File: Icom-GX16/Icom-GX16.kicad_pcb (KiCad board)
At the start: 2 copper layers, 27.3 x 30.5 mm, 6 parts, among them J1 Mic Input, J2 Base Board, J3 Headphone/Speaker Input

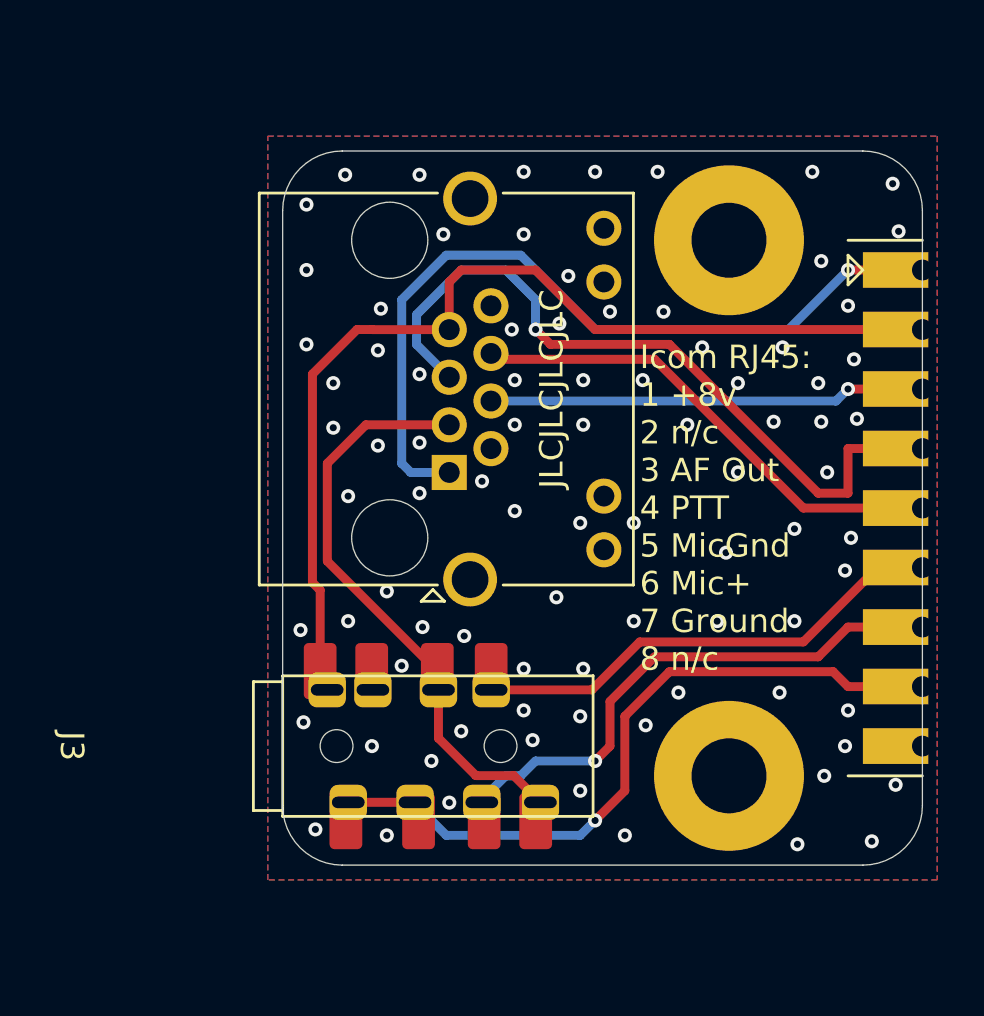
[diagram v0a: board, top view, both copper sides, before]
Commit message: Icom-GX16 added. Also GX16 riser board. #1
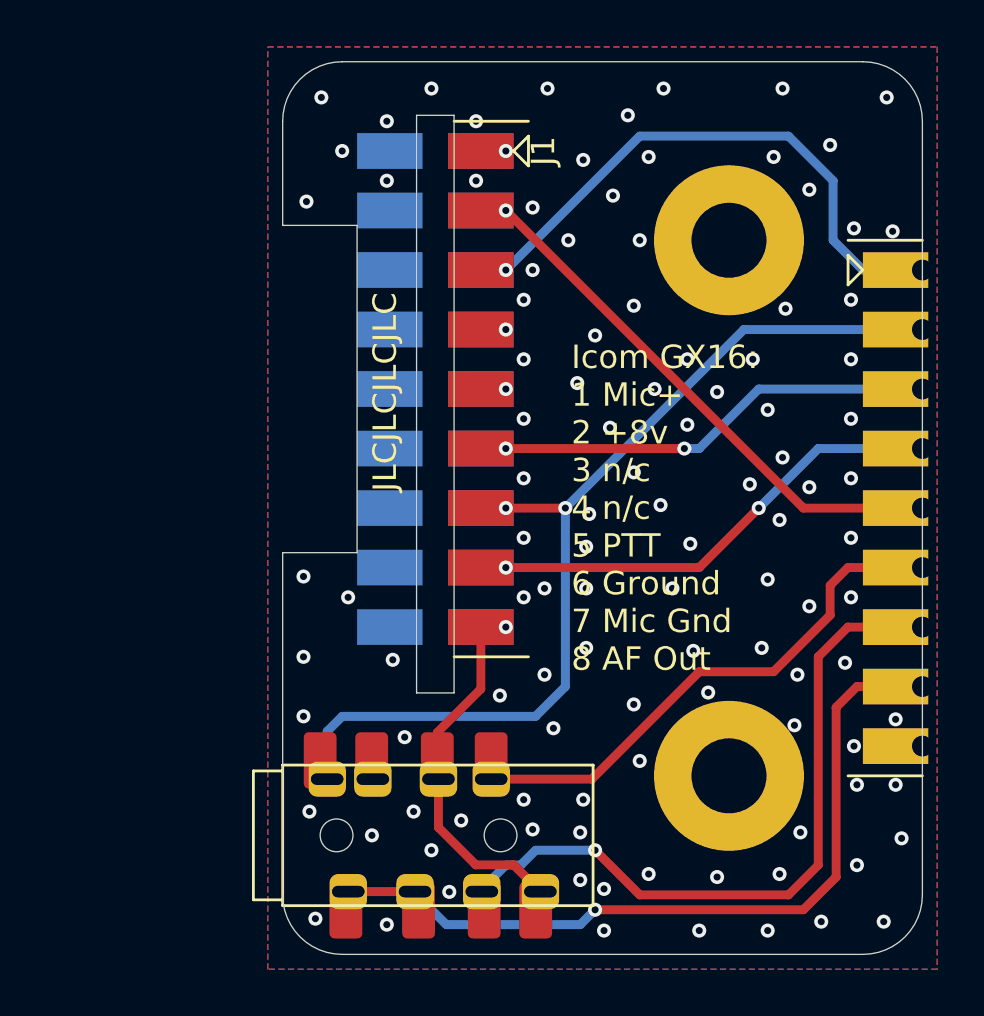
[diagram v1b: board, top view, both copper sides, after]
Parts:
- removed G1: Logo_OHIS, OHIS:Logo_OHIS_Medium
- added J4: Icom GX16 Board, Libraries:Conn_B2B-RA_2.54mm_9pin_LtoR, F.Cu at (70.8, 73.7)
- added J5: Icom GX16 Board, Libraries:Conn_B2B-RA_2.54mm_9pin_LtoR, B.Cu at (69.2, 73.7)
- J1: value Mic Input -> Icom GX16 Board; footprint Connector_RJ:RJ45_Amphenol_RJHSE538X -> Libraries:Conn_B2B-RA_2.54mm_9pin_RtoL; moved to B.Cu
- moved J3 3.81 mm to (63.5, 92.7)
- moved J1 3.57 mm to (70.8, 73.7)
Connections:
- J1 pad 1: +8v 10mA -> Shield
- J1 pad 2: Freq Up/Down -> Mic+
- J1 pad 3: AF Out -> +8v 10mA
- J1 pad 4: ~{PTT} -> Freq Up/Down
- J1 pad 5: Mic Gnd -> ~{SQL Open}
- J1 pad 6: Mic+ -> ~{PTT}
- J1 pad 8: ~{SQL Open} -> Mic Gnd
- J1 pad 9: unconnected-(J1-Pad9) -> AF Out
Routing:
- net Mic Gnd: track 31.1 -> 19.2 mm, vias 1 -> 2
- net AF Out: track 24.2 -> 14.0 mm, vias 0 -> 1
- net +8v 10mA: track 33.4 -> 23.3 mm
- net HP Right: track 21.9 -> 29.6 mm
- net HP Gnd: track 29.0 -> 32.9 mm
- net HP Left: track 19.4 -> 23.0 mm
- net Mic+: track 20.0 -> 22.4 mm, vias 0 -> 1
- net ~{PTT}: track 17.5 -> 18.1 mm, vias 1 -> 2
- net Power Gnd: track 41.8 -> 41.9 mm, vias 0 -> 2
- net ~{SQL Open}: vias 0 -> 1
- net Shield: vias 86 -> 110
- net Freq Up/Down: vias 0 -> 1
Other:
- board size 27.3 x 30.5 mm -> 27.3 x 38.1 mm
- board text added: "Icom GX16: 1 Mic+ 2 +8v 3 n/c 4 n/c 5 PTT 6 Ground 7 Mic Gnd 8 AF Out"
- board text added: "OHIS Radio Adapter v1.0a, Icom - GX16"
- board text removed: "Icom RJ45: 1 +8v 2 n/c 3 AF Out 4 PTT 5 MicGnd 6 Mic+ 7 Ground 8 n/c"
- board text removed: "OHIS Radio Adapter v1.0a, Icom - RJ45"
